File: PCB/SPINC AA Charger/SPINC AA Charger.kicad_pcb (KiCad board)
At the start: 4 copper layers, 70 x 72 mm, 101 parts, among them J1 USB_C_Receptacle_USB2.0, J2 Conn_01x03_Pin, J3 Conn_01x10_Socket, J4 Conn_01x01_Pin, J5 Conn_01x01_Pin, Q1 DMG2301L, Q2 DMHC3025LSD, Q3 DMG2301L, Q4 DMG2301L, Q5 SI2305CDS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

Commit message: Small fixes for the PCB
- Changed fuse from 500mA to 1A (when charging at full 1A, the device draws slightly more than 500mA)
- Changed R32 from 80k to 22k (somehow the cell check fails with 100mV sensitivity)
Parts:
- F1: value 500mA -> 1A
- R32: value 82k -> 22k

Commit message: WIP: initial pcb placement
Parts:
- removed C10, C13, C14, C16, C18, C19, C21, C22, C24: 100nF, Capacitor_SMD:C_0603_1608Metric
- removed C11, C12: 15pF, Capacitor_SMD:C_0603_1608Metric
- removed C17, C20: 1uF, Capacitor_SMD:C_0603_1608Metric
- removed R2: 1k, Resistor_SMD:R_0603_1608Metric
- removed R7, R8: 27, Resistor_SMD:R_0603_1608Metric
- removed R9: 10k, Resistor_SMD:R_0603_1608Metric
- removed SW2: SW_Push, Button_Switch_SMD:SW_SPST_EVQP2
- removed TP1: TestPoint, TestPoint:TestPoint_Pad_D1.5mm
- removed U5: RP2040, Package_DFN_QFN:QFN-56-1EP_7x7mm_P0.4mm_EP3.2x3.2mm
- removed Y1: ABM8-272-T3, Crystal:Crystal_SMD_Abracon_ABM8G-4Pin_3.2x2.5mm
- added C23: 1uF, Capacitor_SMD:C_0603_1608Metric, F.Cu at (161.5, 110.5)
- added C31: 100nF, Capacitor_SMD:C_0603_1608Metric, F.Cu at (176.0, 78.5)
- added R1: 10k, Resistor_SMD:R_0603_1608Metric, F.Cu at (161.5, 112.0)
- added U6: ESP32-WROOM-32U, RF_Module:ESP32-WROOM-32U, F.Cu at (172.9, 115.8)
- C6: value 1uF -> 10uF
- U3: value W25Q64JVZPIQ -> CH340N; footprint Package_SON:WSON-8-1EP_6x5mm_P1.27mm_EP3.4x4.3mm -> Package_SO:SOP-8_3.9x4.9mm_P1.27mm
- moved U3 32.9 mm to (170.5, 76.5)
- moved D1 10.6 mm to (163.0, 133.2)
- moved D5 10.6 mm to (163.0, 130.2)
- moved R10 10.6 mm to (161.5, 130.2)
- moved R14 10.6 mm to (161.5, 133.2)
- moved C6 6.10 mm to (162.0, 108.3), turned to 90 degrees
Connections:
- U3 pad 1: QSPI_CS -> USB_D_P
- U3 pad 2: QSPI_SD1 -> USB_D_N
- U3 pad 3: QSPI_SD2 -> GND
- U3 pad 4: GND -> unconnected-(U3-~{RTS}-Pad4)
- U3 pad 5: QSPI_SD0 -> +3V3
- U3 pad 6: QSPI_SCLK -> RX
- U3 pad 7: QSPI_SD3 -> TX
- U3 pad 8: +3.3V -> +3V3
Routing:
- net USB_D_N: track 56.5 -> 0.96 mm
- net USB_D_P: track 56.8 -> 1.69 mm
- net Net-(R2-Pad2): track 51.5 -> 0.00 mm, vias 2 -> 0
- net +3.3V: track 62.0 -> 27.9 mm, vias 17 -> 9
- net VCN_INT: track 81.4 -> 52.8 mm, vias 2 -> 1
- net +1V1: track 27.3 -> 0.00 mm, vias 2 -> 0
- net SDA: track 85.7 -> 58.5 mm, vias 2 -> 1
- net ADC_TEMP_BAT: track 31.3 -> 6.76 mm, vias 2 -> 1
- net SW_2: track 104.8 -> 82.6 mm, vias 2 -> 1
- net SCL: track 83.6 -> 61.6 mm, vias 2 -> 1
- net SW_1: track 67.6 -> 48.8 mm, vias 2 -> 1
- net QSPI_CS: track 18.6 -> 0.00 mm
- net LCD_CS: track 25.2 -> 8.86 mm
- net LCD_MOSI: track 24.2 -> 8.21 mm
- net LCD_SCK: track 23.1 -> 7.62 mm
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
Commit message: Route everything
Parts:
- moved C23 3.50 mm to (161.5, 114.0)
- moved C31 1.00 mm to (177.0, 78.5)
- moved R1 1.00 mm to (161.5, 111.0)
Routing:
- net RX: track 0.00 -> 47.4 mm
- net TX: track 0.00 -> 46.0 mm
- net LCD_CS: track 8.86 -> 44.7 mm, vias 0 -> 2
- net +3.3V: track 27.9 -> 62.3 mm, vias 9 -> 11
- net LCD_MOSI: track 8.21 -> 42.6 mm, vias 0 -> 2
- net ADC_TEMP_BAT: track 6.76 -> 36.9 mm, vias 1 -> 2
- net HBR_BH: track 32.6 -> 61.4 mm, vias 1 -> 3
- net VCN_INT: track 52.8 -> 80.4 mm, vias 1 -> 2
- net LCD_SCK: track 7.62 -> 34.6 mm, vias 0 -> 2
- net SW_1: track 48.8 -> 72.3 mm, vias 1 -> 2
- net SW_2: track 82.6 -> 104.5 mm, vias 1 -> 2
- net HBR_AL: track 43.7 -> 64.7 mm, vias 1 -> 2
- net USB_D_P: track 1.69 -> 22.6 mm
- net HBR_AH: track 30.3 -> 48.2 mm, vias 1 -> 2
- net USB_D_N: track 0.96 -> 17.2 mm
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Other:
- board text added: "AA Charger Rev. ESP-1 Maximilian Kern Mads Chr. Olesen 12/2024"
- board text removed: "AA Charger Rev. 2 Maximilian Kern 10/2024"

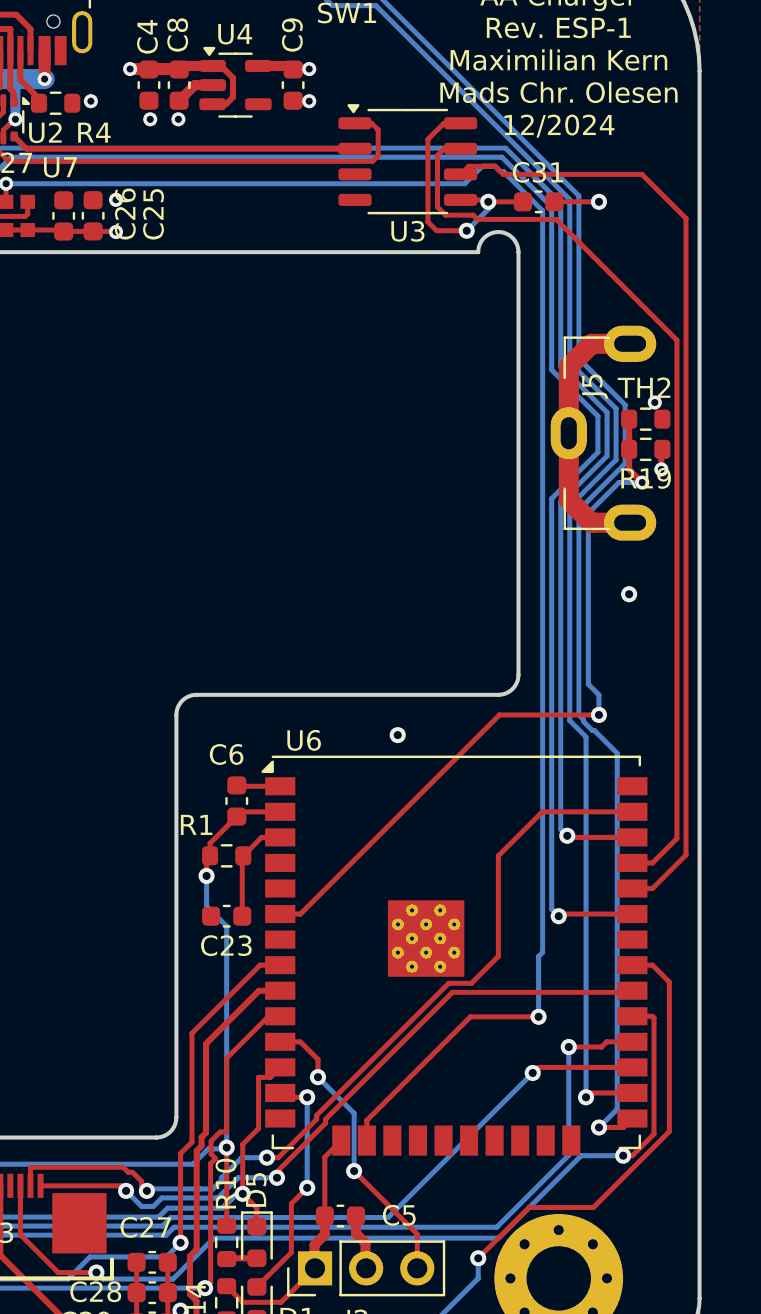
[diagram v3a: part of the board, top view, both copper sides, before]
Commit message: Optimize a little routing
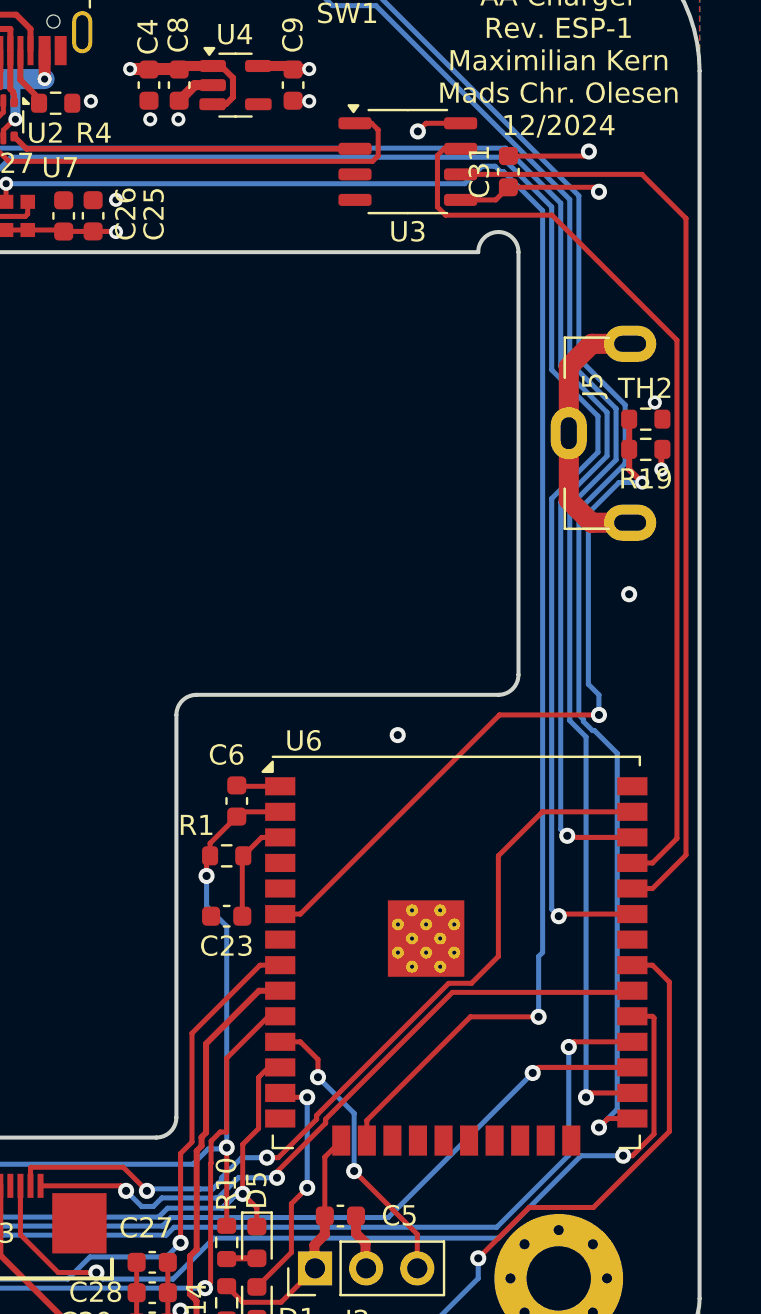
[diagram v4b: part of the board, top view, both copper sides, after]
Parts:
- moved C31 2.12 mm to (175.5, 77.0), turned to 90 degrees
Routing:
- net +3V3: track 13.3 -> 9.66 mm
- net GND: track 36.6 -> 38.5 mm
